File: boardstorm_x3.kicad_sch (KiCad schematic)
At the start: 0 parts

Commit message: worked on capacitors, wiring and usb c
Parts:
- added C1, C10: 1uF, symbol Device:C
- added C11, C12, C2, C3, C4, C5, C6, C7, C8, C9: 0.1uF, symbol Device:C
- added C13, C14: 10uF, symbol Device:C
- added J1: USB_C_Receptacle_USB2.0_14P, symbol Connector:USB_C_Receptacle_USB2.0_14P
- added R1, R2: 5.1K, symbol Device:R
- added U1: RP2040, Package_DFN_QFN:QFN-56-1EP_7x7mm_P0.4mm_EP3.2x3.2mm, symbol MCU_RaspberryPi:RP2040
- added U2: NCP1117-3.3_SOT223, Package_TO_SOT_SMD:SOT-223-3_TabPin2, symbol Regulator_Linear:NCP1117-3.3_SOT223
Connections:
- new net: C14.1, U2.2 (VO)
- new net: C13.1, J1.A4 (VBUS), J1.A9 (VBUS), J1.B4 (VBUS), J1.B9 (VBUS), U2.3 (VI)
- new net: J1.A5 (CC1), R1.1
- new net: J1.B5 (CC2), R2.1
- new net +1V1: C10.1, C11.1, C12.1, U1.23 (DVDD), U1.45 (VREG_VOUT), U1.50 (DVDD)
- new net +3V3: C1.1, C2.1, C3.1, C4.1, C5.1, C6.1, C7.1, C8.1, C9.1, U1.1 (IOVDD), U1.10 (IOVDD), U1.22 (IOVDD), U1.33 (IOVDD), U1.42 (IOVDD), U1.43 (ADC_AVDD), U1.44 (VREG_VIN), U1.48 (USB_VDD), U1.49 (IOVDD)
- new net GND: C1.2, C10.2, C11.2, C12.2, C13.2, C14.2, C2.2, C3.2, C4.2, C5.2, C6.2, C7.2, C8.2, C9.2, J1.A1 (GND), J1.A12 (GND), J1.B1 (GND), J1.B12 (GND), J1.SH (SHIELD), R1.2, R2.2, U2.1 (GND)
- new net USB_D+: J1.A6 (D+), J1.B6 (D+)
- new net USB_D-: J1.A7 (D-), J1.B7 (D-)

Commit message: setting up a crystal oscillator system, studied more about usbc power and the clock mechanism in such tiny boards.
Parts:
- added C15, C16: 15pF, symbol Device:C
- added R3, R4: 27, symbol Device:R
- added R5: 5K, symbol Device:R
- added Y1: 12 MHz, symbol Device:Crystal_GND24
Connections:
- net +3V3: now also C14.1, U2.2 (VO)
- net GND: now also C15.1, C16.1, Y1.2 (G), Y1.4 (G)
- net USB_D+: now also R4.2
- net USB_D-: now also R3.2
- net VBUS: now reaches C13.1, J1.A4 (VBUS), J1.A9 (VBUS), J1.B4 (VBUS), J1.B9 (VBUS), U2.3 (VI)
- net XIN: now reaches U1.20 (XIN)
- net XIN: now also C15.2, Y1.3
- net XOUT: now reaches U1.21 (XOUT)
- net XOUT: now also R5.2
- net at U1.46 (USB_DM): now also R3.1
- net at U1.47 (USB_DP): now also R4.1
- net QSPI_SD3: now reaches U1.51 (QSPI_SD3)
- net QSPI_SCLK: now reaches U1.52 (QSPI_SCLK)
- net QSPI_SD0: now reaches U1.53 (QSPI_SD0)
- net QSPI_SD2: now reaches U1.54 (QSPI_SD2)
- net QSPI_SD1: now reaches U1.55 (QSPI_SD1)
- net QSPI_SS: now reaches U1.56 (~{QSPI_SS})
- new net: C16.2, R5.1, Y1.1
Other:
- moved on the sheet: C13, C14, U2

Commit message: done with flash storage & more progress YAHOO
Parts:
- added C17: 0.1uF, symbol Device:C
- added R6: 1K, symbol Device:R
- added R7: 10K, symbol Device:R
- added SW1: SW_Push, symbol Switch:SW_Push
- added U3: W25Q128JVS, Package_SO:SOIC-8_5.3x5.3mm_P1.27mm, symbol Memory_Flash:W25Q128JVS
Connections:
- net +3V3: now also C17.1, R7.2, U3.8 (VCC)
- net GND: now also U1.19 (TESTEN), U1.57 (GND), C17.2, SW1.1, U3.4 (GND)
- net QSPI_SCLK: now also U3.6 (CLK)
- net QSPI_SD0: now also U3.5 (DI/IO_{0})
- net QSPI_SD1: now also U3.2 (DO/IO_{1})
- net QSPI_SD2: now also U3.3 (~{WP}/IO_{2})
- net QSPI_SD3: now also U3.7 (~{HOLD}/~{RESET}/IO_{3})
- net QSPI_SS: now also R6.2, R7.1, U3.1 (~{CS})
- net GPIO8: now reaches U1.11 (GPIO8)
- net GPIO9: now reaches U1.12 (GPIO9)
- net GPIO10: now reaches U1.13 (GPIO10)
- net GPIO11: now reaches U1.14 (GPIO11)
- net GPIO12: now reaches U1.15 (GPIO12)
- net GPIO13: now reaches U1.16 (GPIO13)
- net GPIO14: now reaches U1.17 (GPIO14)
- net GPIO15: now reaches U1.18 (GPIO15)
- net GPIO0: now reaches U1.2 (GPIO0)
- net SWCLK: now reaches U1.24 (SWCLK)
- net SWDIO: now reaches U1.25 (SWDIO)
- net RUN: now reaches U1.26 (RUN)
- net GPIO16: now reaches U1.27 (GPIO16)
- net GPIO17: now reaches U1.28 (GPIO17)
- net GPIO18: now reaches U1.29 (GPIO18)
- net GPIO1: now reaches U1.3 (GPIO1)
- net GPIO19: now reaches U1.30 (GPIO19)
- net GPIO20: now reaches U1.31 (GPIO20)
- net GPIO21: now reaches U1.32 (GPIO21)
- net GPIO22: now reaches U1.34 (GPIO22)
- net GPIO23: now reaches U1.35 (GPIO23)
- net GPIO24: now reaches U1.36 (GPIO24)
- net GPIO25: now reaches U1.37 (GPIO25)
- net GPIO26/ADC0: now reaches U1.38 (GPIO26/ADC0)
- net GPIO26/ADC1: now reaches U1.39 (GPIO27/ADC1)
- net GPIO2: now reaches U1.4 (GPIO2)
- net GPIO26/ADC2: now reaches U1.40 (GPIO28/ADC2)
- net GPIO26/ADC3: now reaches U1.41 (GPIO29/ADC3)
- net GPIO3: now reaches U1.5 (GPIO3)
- net GPIO4: now reaches U1.6 (GPIO4)
- net GPIO5: now reaches U1.7 (GPIO5)
- net GPIO6: now reaches U1.8 (GPIO6)
- net GPIO7: now reaches U1.9 (GPIO7)
- new net: R6.1, SW1.2
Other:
- moved on the sheet: C15, C16, R3, R4, R5

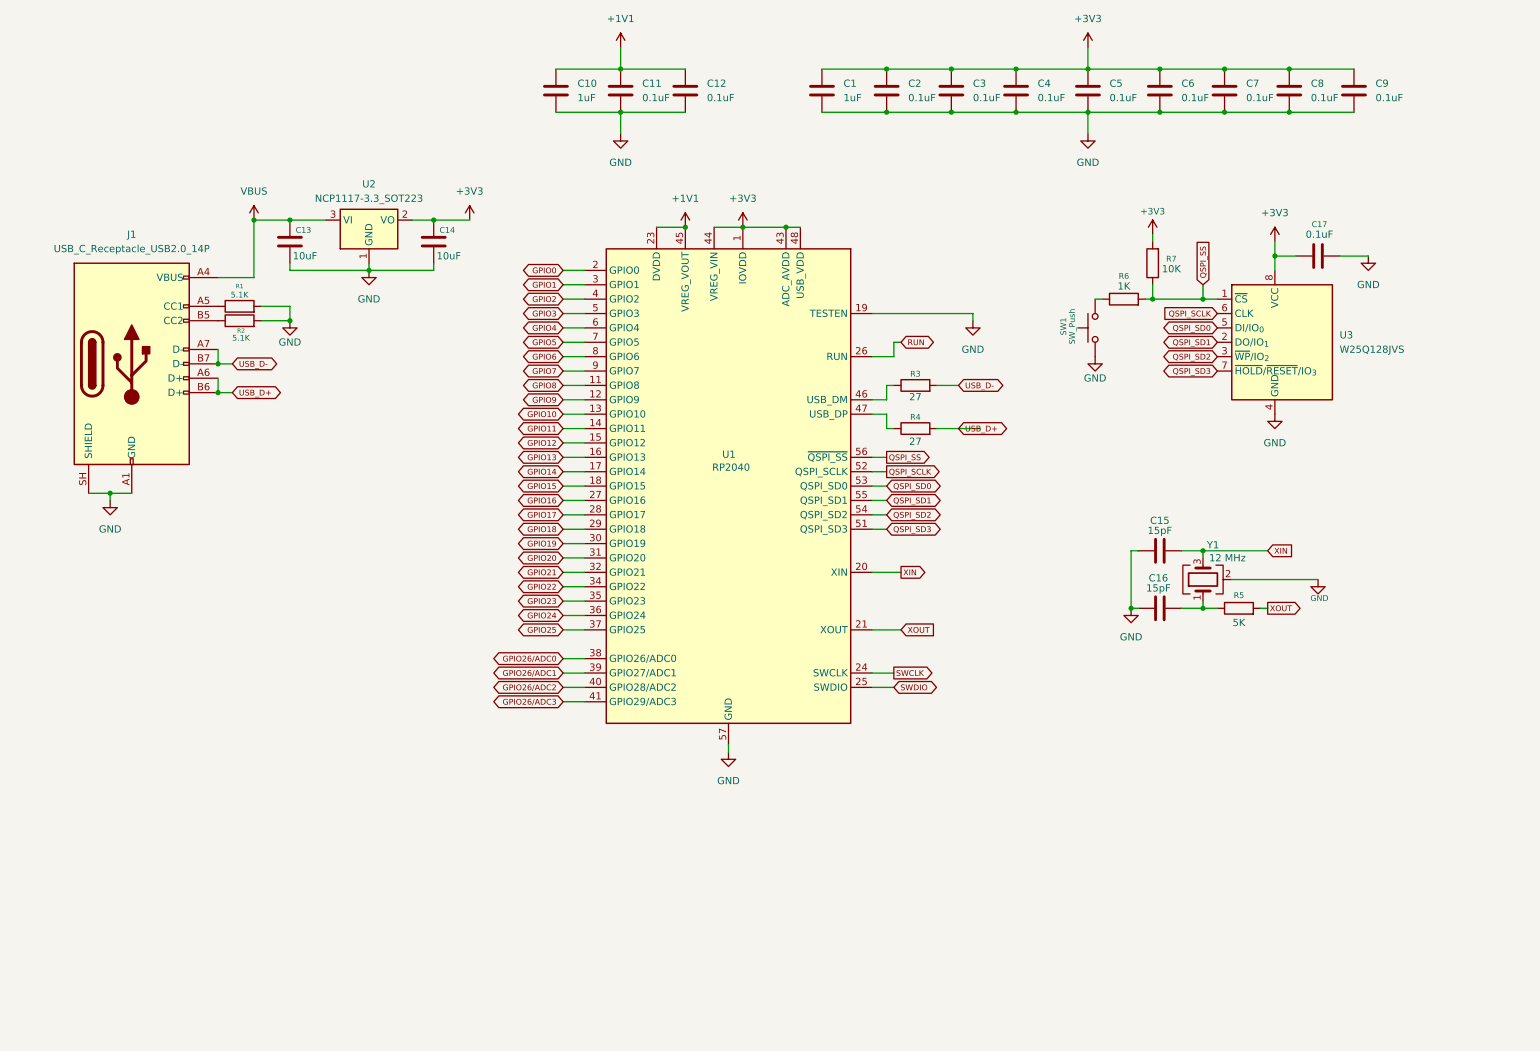
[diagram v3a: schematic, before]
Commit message: added header pin symbols & finished up the schematic design
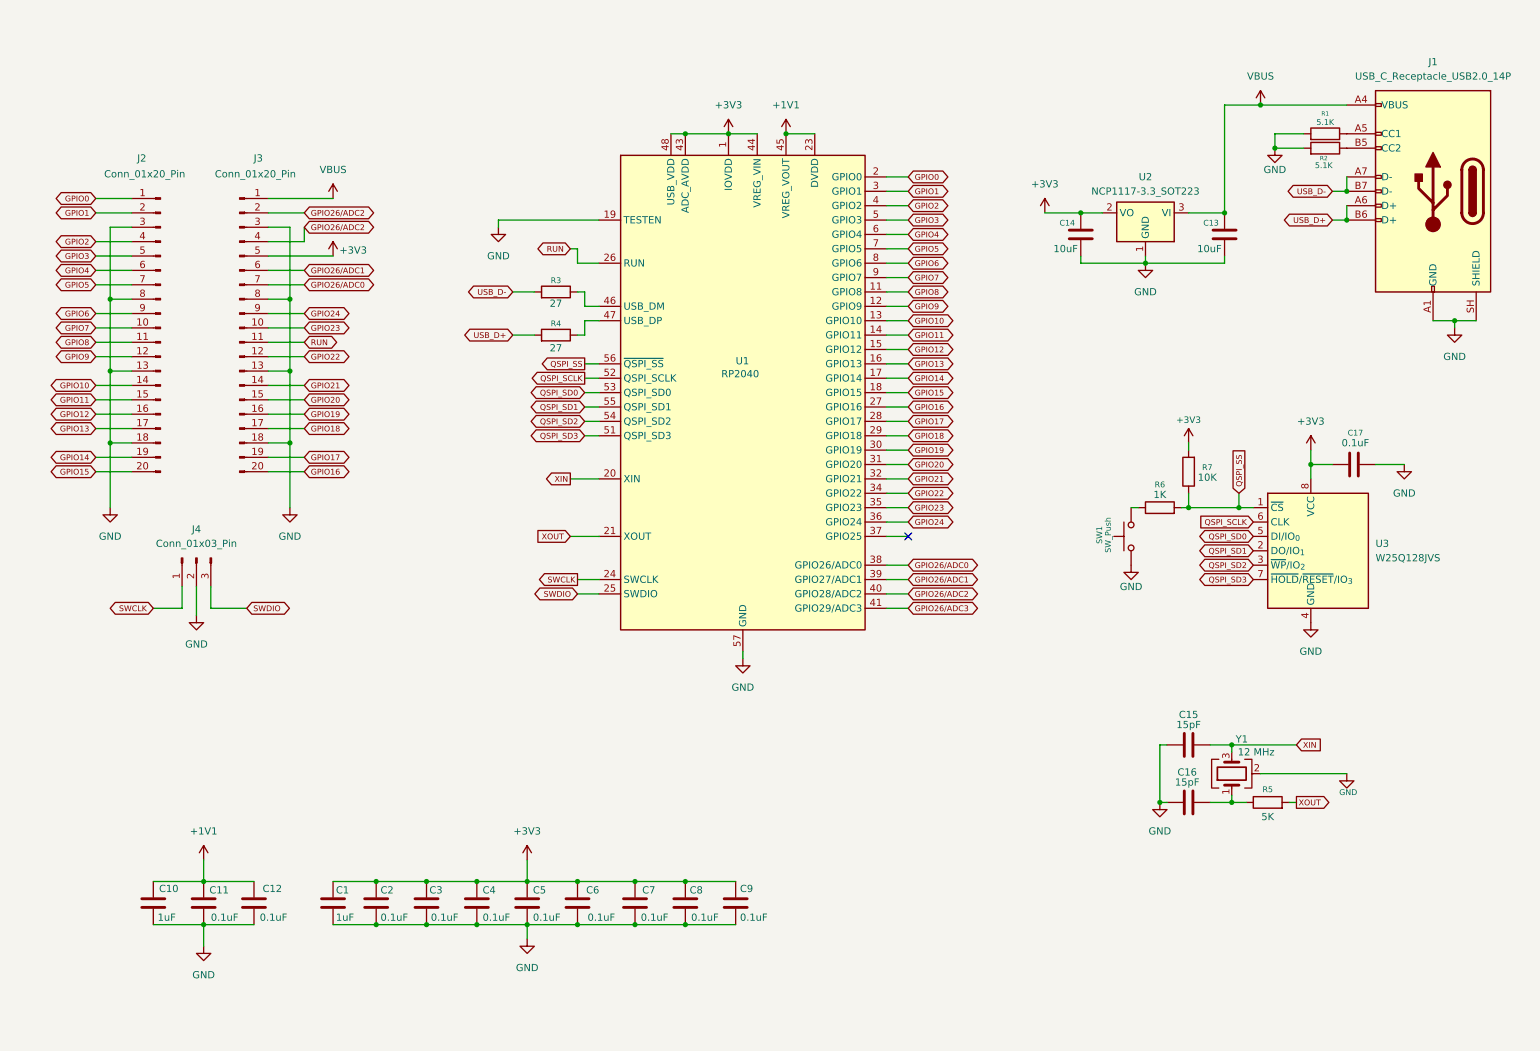
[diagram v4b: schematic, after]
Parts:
- added J2, J3: Conn_01x20_Pin, symbol Connector:Conn_01x20_Pin
- added J4: Conn_01x03_Pin, symbol Connector:Conn_01x03_Pin
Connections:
- net +3V3: now also J3.5 (Pin_5)
- net GND: now also J2.13 (Pin_13), J2.18 (Pin_18), J2.3 (Pin_3), J2.8 (Pin_8), J3.13 (Pin_13), J3.18 (Pin_18), J3.3 (Pin_3), J3.8 (Pin_8), J4.2 (Pin_2)
- net GPIO0: now also J2.1 (Pin_1)
- net GPIO1: now also J2.2 (Pin_2)
- net GPIO10: now also J2.14 (Pin_14)
- net GPIO11: now also J2.15 (Pin_15)
- net GPIO12: now also J2.16 (Pin_16)
- net GPIO13: now also J2.17 (Pin_17)
- net GPIO14: now also J2.19 (Pin_19)
- net GPIO15: now also J2.20 (Pin_20)
- net GPIO16: now also J3.20 (Pin_20)
- net GPIO17: now also J3.19 (Pin_19)
- net GPIO18: now also J3.17 (Pin_17)
- net GPIO19: now also J3.16 (Pin_16)
- net GPIO2: now also J2.4 (Pin_4)
- net GPIO20: now also J3.15 (Pin_15)
- net GPIO21: now also J3.14 (Pin_14)
- net GPIO22: now also J3.12 (Pin_12)
- net GPIO23: now also J3.10 (Pin_10)
- net GPIO24: now also J3.9 (Pin_9)
- net GPIO26/ADC0: now also J3.7 (Pin_7)
- net GPIO26/ADC1: now also J3.6 (Pin_6)
- net GPIO26/ADC2: now also J3.2 (Pin_2), J3.4 (Pin_4)
- net GPIO3: now also J2.5 (Pin_5)
- net GPIO4: now also J2.6 (Pin_6)
- net GPIO5: now also J2.7 (Pin_7)
- net GPIO6: now also J2.9 (Pin_9)
- net GPIO7: now also J2.10 (Pin_10)
- net GPIO8: now also J2.11 (Pin_11)
- net GPIO9: now also J2.12 (Pin_12)
- net RUN: now also J3.11 (Pin_11)
- net SWCLK: now also J4.1 (Pin_1)
- net SWDIO: now also J4.3 (Pin_3)
- net VBUS: now also J3.1 (Pin_1)
- net GPIO25: no longer names the net of U1.37 (GPIO25)
- no-connect marks 0 -> 1
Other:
- moved on the sheet: C1, C10, C11, C12, C13, C14, C15, C16, C17, C2, C3, C4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

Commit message: fixed  a few issues/typos
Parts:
- removed U2: NCP1117-3.3_SOT223, Package_TO_SOT_SMD:SOT-223-3_TabPin2, symbol Regulator_Linear:NCP1117-3.3_SOT223
- removed U3: W25Q128JVS, Package_SO:SOIC-8_5.3x5.3mm_P1.27mm, symbol Memory_Flash:W25Q128JVS
- added U2: MCP1700x-330xxTT, Package_TO_SOT_SMD:SOT-23, symbol Regulator_Linear:MCP1700x-330xxTT
- added U3: W25Q16JVSS, Package_SO:SOIC-8_5.3x5.3mm_P1.27mm, symbol Memory_Flash:W25Q16JVSS
- C15, C16: value 15pF -> 33pF
- R5: value 5K -> 1K
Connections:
- net +3V3: now also U2.2 (VO), U3.8 (VCC)
- net GND: now also U2.1 (GND), U3.4 (GND)
- net QSPI_SCLK: now also U3.6 (CLK)
- net QSPI_SD0: now also U3.5 (DI/IO_{0})
- net QSPI_SD1: now also U3.2 (DO/IO_{1})
- net QSPI_SD2: now also U3.3 (~{WP}/IO_{2})
- net QSPI_SD3: now also U3.7 (~{HOLD}/~{RESET}/IO_{3})
- net QSPI_SS: now also U3.1 (~{CS})
- net VBUS: now also U2.3 (VI)
- net GPIO26/ADC1 renamed GPIO27/ADC1
- net GPIO26/ADC2 renamed GPIO28/ADC2
- net GPIO28/ADC2: no longer J3.2 (Pin_2)
- net GPIO26/ADC3 renamed GPIO29/ADC3
- net GPIO29/ADC3: now also J3.2 (Pin_2)
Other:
- moved on the sheet: C15, C16, C17, R5, R6, R7, SW1, Y1

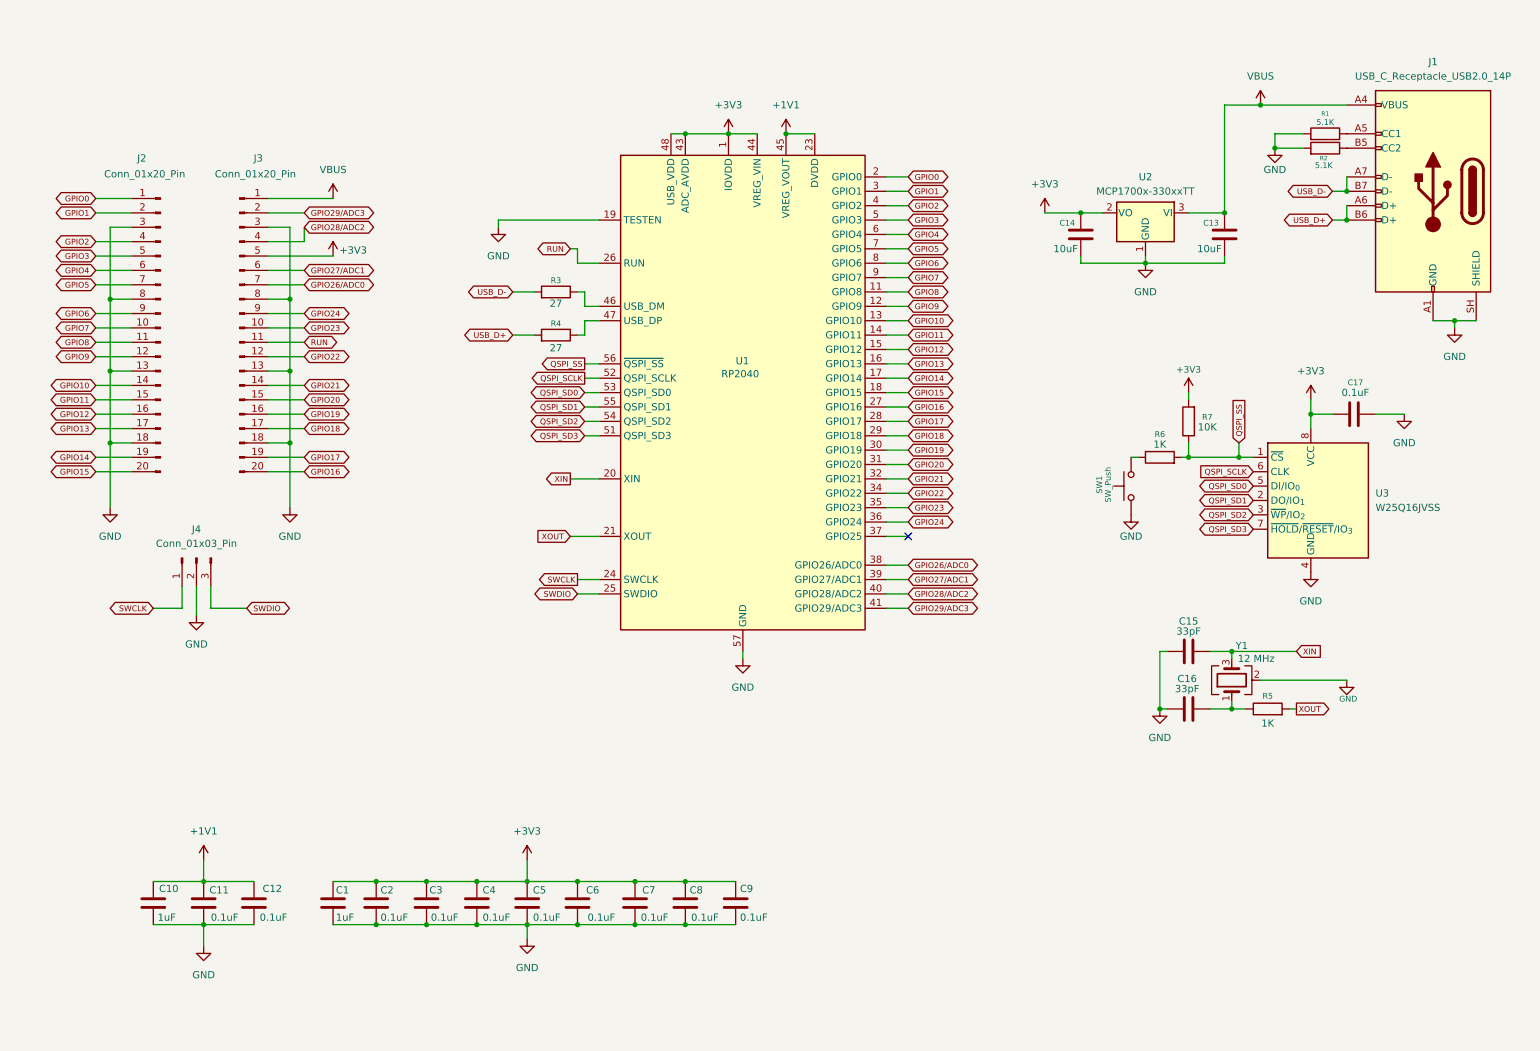
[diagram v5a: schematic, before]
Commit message: making some progress... using a power path with the usb c input
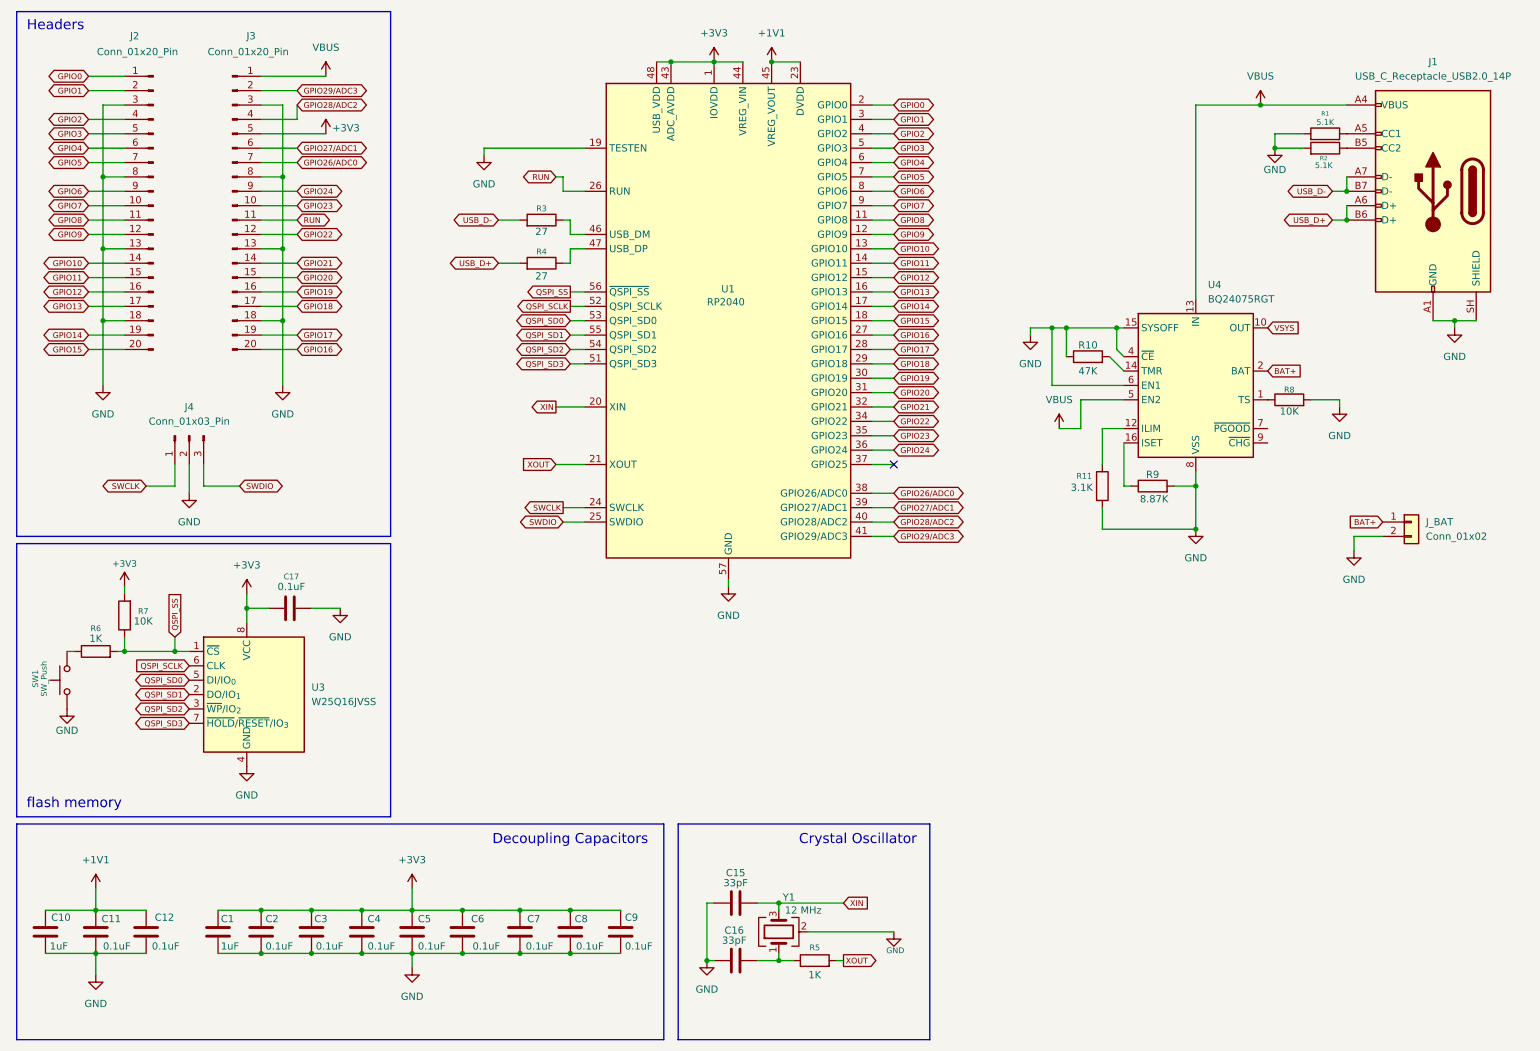
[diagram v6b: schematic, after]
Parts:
- removed C13, C14: 10uF, symbol Device:C
- removed U2: MCP1700x-330xxTT, Package_TO_SOT_SMD:SOT-23, symbol Regulator_Linear:MCP1700x-330xxTT
- added J_BAT: Conn_01x02, symbol Connector_Generic:Conn_01x02
- added R10: 47K, symbol Device:R
- added R11: 3.1K, symbol Device:R
- added R8: 10K, symbol Device:R
- added R9: 8.87K, symbol Device:R
- added U4: BQ24075RGT, Package_DFN_QFN:VQFN-16-1EP_3x3mm_P0.5mm_EP1.6x1.6mm, symbol Battery_Management:BQ24075RGT
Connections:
- net GND: now also J_BAT.2 (Pin_2), R10.1, R11.2, R8.2, R9.2, U4.15 (SYSOFF), U4.17 (VSS), U4.4 (~{CE}), U4.6 (EN1), U4.8 (VSS)
- net VBUS: now also U4.13 (IN), U4.5 (EN2)
- new net: R8.1, U4.1 (TS)
- new net: R11.1, U4.12 (ILIM)
- new net: R10.2, U4.14 (TMR)
- new net: R9.1, U4.16 (ISET)
- new net BAT+: J_BAT.1 (Pin_1), U4.2 (BAT), U4.3 (BAT)
- new net VSYS: U4.10 (OUT), U4.11 (OUT)
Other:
- note added: "Crystal Oscillator"
- note added: "Decoupling Capacitors"
- note added: "Headers"
- note added: "flash memory"
- moved on the sheet: C1, C10, C11, C12, C15, C16, C17, C2, C3, C4, C5, C6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

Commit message: backing up
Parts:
- added C13, C18: 10uF, symbol Device:C
- added C14: 4.7uF, symbol Device:C
- added U2: MCP1700x-330xxTT, Package_TO_SOT_SMD:SOT-23, symbol Regulator_Linear:MCP1700x-330xxTT
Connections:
- net +3V3: now also U2.2 (VO)
- net BAT+: now also C14.1
- net GND: now also C13.2, C14.2, C18.2, U2.1 (GND)
- net VBUS: now also C13.1
- net VSYS: now also C18.1, U2.3 (VI)
- no-connect marks 1 -> 3
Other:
- moved on the sheet: J_BAT, R10, R11, R8, R9, U4
